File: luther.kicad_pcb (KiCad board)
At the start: 2 copper layers, 114 x 50 mm, 0 parts

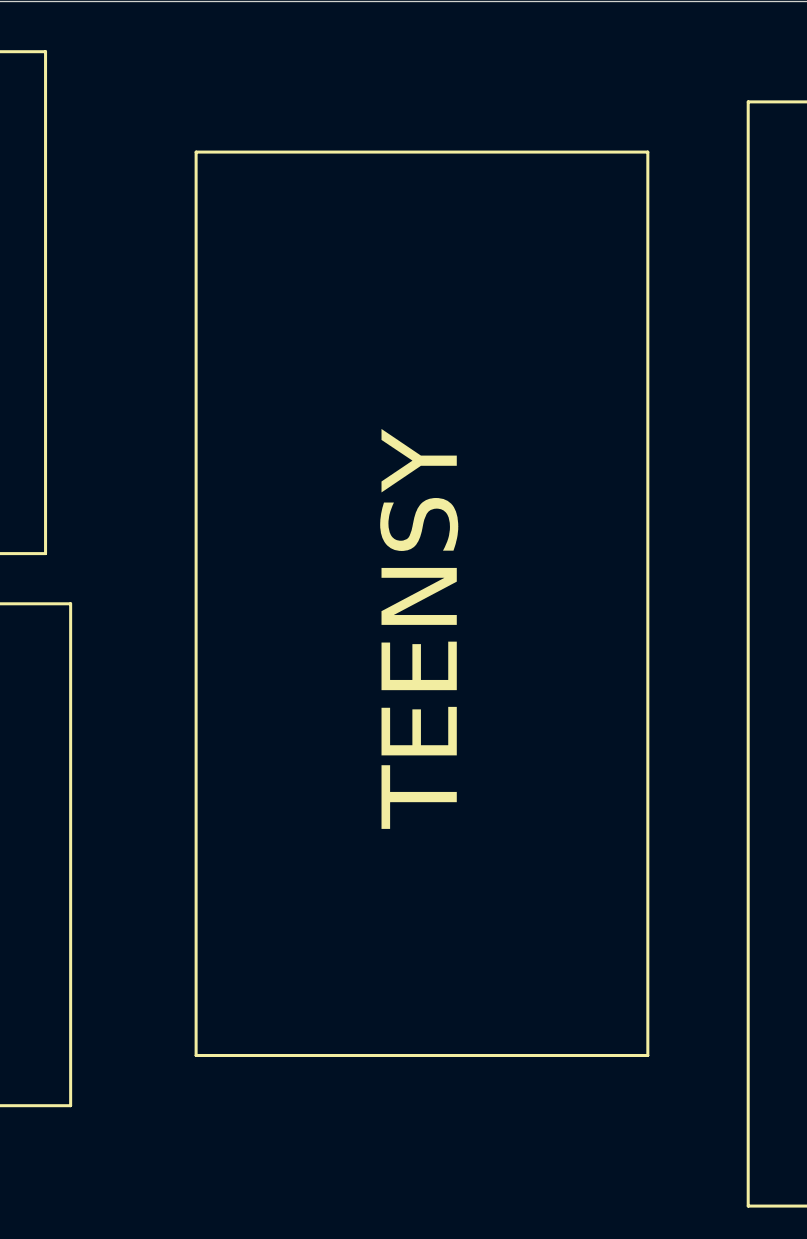
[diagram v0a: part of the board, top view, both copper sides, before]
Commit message: add teensy footprint
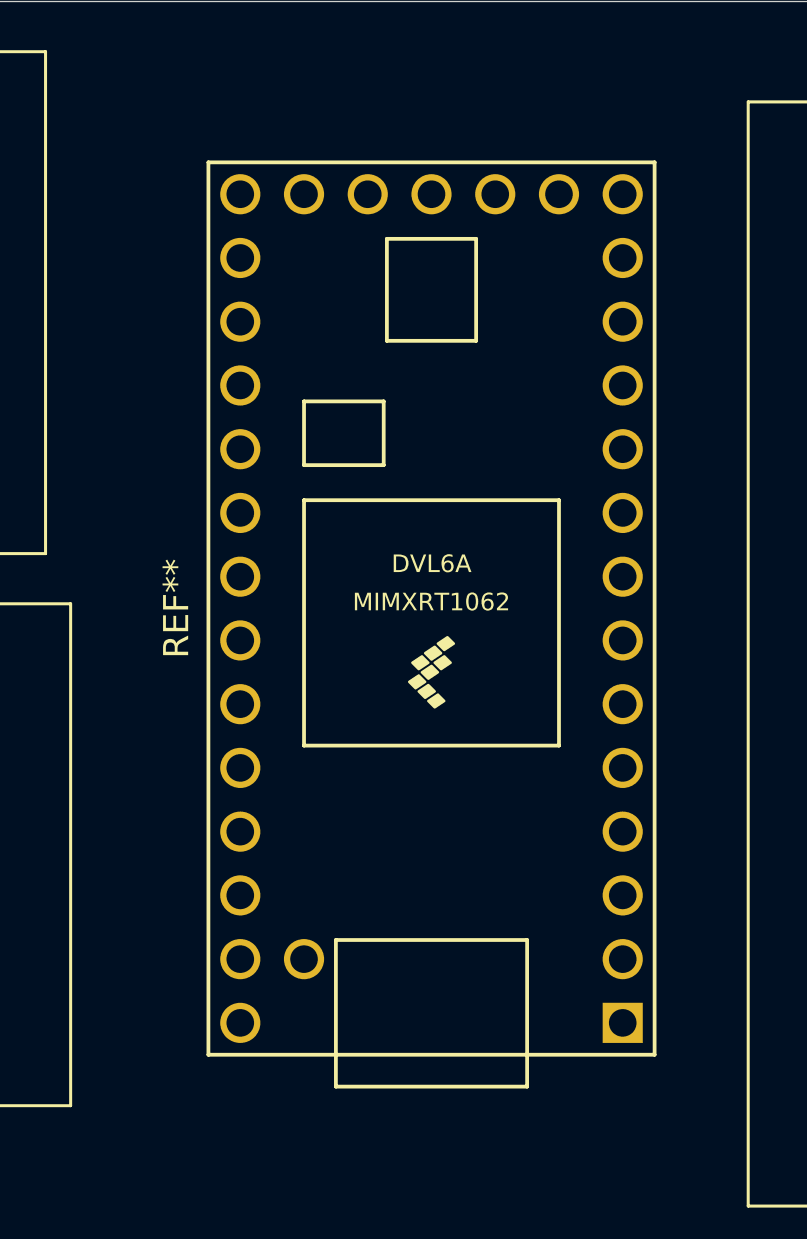
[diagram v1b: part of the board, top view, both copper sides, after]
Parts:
- added REF**: Teensy4.0, libs:Teensy40, F.Cu at (86.4, 94.2)
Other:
- board text removed: "TEENSY"
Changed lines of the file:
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@@
   (general
     (thickness 1.6)
-    (drawings 62)
+    (drawings 57)
     (tracks 0)
     (zones 0)
-    (modules 0)
+    (modules 1)
     (nets 1)
   )
@@
     (solder_mask_min_width 0.25)
     (aux_axis_origin 0 0)
-    (visible_elements FFFFFF7F)
+    (visible_elements 7FFFFFFF)
     (pcbplotparams
       (layerselection 0x010fc_ffffffff)
@@
     (uvia_drill 0.1)
   )
+  (module libs:Teensy40 (layer F.Cu)
+    (at 86.38 94.19 90)
+    (fp_text reference REF** (at 0 -10.16 90) (layer F.SilkS)
+      (effects (font (size 1 1) (thickness 0.15)))
+    )
+    (fp_text value Teensy4.0 (at 0 10.16 90) (layer F.Fab)
+      (effects (font (size 1 1) (thickness 0.15)))
+    )
+    (fp_text user DVL6A (at 1.778 0) (layer F.SilkS)
+      (effects (font (size 0.7 0.7) (thickness 0.15)))
+    )
+    (fp_poly (pts (xy -3.937 0.127) (xy -3.683 -0.127) (xy -3.429 0.254) (xy -3.683 0.508)) (layer F.SilkS) (width 0.1))
+    (fp_poly (pts (xy -3.556 -0.254) (xy -3.302 -0.508) (xy -3.048 -0.127) (xy -3.302 0.127)) (layer F.SilkS) (width 0.1))
+    (fp_poly (pts (xy -1.651 0.508) (xy -1.397 0.254) (xy -1.143 0.635) (xy -1.397 0.889)) (layer F.SilkS) (width 0.1))
+    (fp_poly (pts (xy -2.032 0) (xy -1.778 -0.254) (xy -1.524 0.127) (xy -1.778 0.381)) (layer F.SilkS) (width 0.1))
+    (fp_poly (pts (xy -2.413 -0.508) (xy -2.159 -0.762) (xy -1.905 -0.381) (xy -2.159 -0.127)) (layer F.SilkS) (width 0.1))
+    (fp_poly (pts (xy -2.413 0.381) (xy -2.159 0.127) (xy -1.905 0.508) (xy -2.159 0.762)) (layer F.SilkS) (width 0.1))
+    (fp_poly (pts (xy -2.794 -0.127) (xy -2.54 -0.381) (xy -2.286 0) (xy -2.54 0.254)) (layer F.SilkS) (width 0.1))
+    (fp_poly (pts (xy -3.175 -0.635) (xy -2.921 -0.889) (xy -2.667 -0.508) (xy -2.921 -0.254)) (layer F.SilkS) (width 0.1))
+    (fp_text user MIMXRT1062 (at 0.254 0) (layer F.SilkS)
+      (effects (font (size 0.7 0.7) (thickness 0.15)))
+    )
+    (fp_line (start 5.715 -1.905) (end 5.715 -5.08) (layer F.SilkS) (width 0.15))
+    (fp_line (start 8.255 -1.905) (end 5.715 -1.905) (layer F.SilkS) (width 0.15))
+    (fp_line (start 8.255 -5.08) (end 8.255 -1.905) (layer F.SilkS) (width 0.15))
+    (fp_line (start 5.715 -5.08) (end 8.255 -5.08) (layer F.SilkS) (width 0.15))
+    (fp_line (start -17.78 8.89) (end -17.78 -8.89) (layer F.SilkS) (width 0.15))
+    (fp_line (start 17.78 8.89) (end -17.78 8.89) (layer F.SilkS) (width 0.15))
+    (fp_line (start 17.78 -8.89) (end 17.78 8.89) (layer F.SilkS) (width 0.15))
+    (fp_line (start -17.78 -8.89) (end 17.78 -8.89) (layer F.SilkS) (width 0.15))
+    (fp_line (start 4.318 5.08) (end -5.461 5.08) (layer F.SilkS) (width 0.15))
+    (fp_line (start 4.318 -5.08) (end -5.461 -5.08) (layer F.SilkS) (width 0.15))
+    (fp_line (start -5.461 -5.08) (end -5.461 5.08) (layer F.SilkS) (width 0.15))
+    (fp_line (start 4.318 5.08) (end 4.318 -5.08) (layer F.SilkS) (width 0.15))
+    (fp_line (start 10.668 -1.778) (end 14.732 -1.778) (layer F.SilkS) (width 0.15))
+    (fp_line (start 10.668 1.778) (end 10.668 -1.778) (layer F.SilkS) (width 0.15))
+    (fp_line (start 14.732 1.778) (end 10.668 1.778) (layer F.SilkS) (width 0.15))
+    (fp_line (start 14.732 -1.778) (end 14.732 1.778) (layer F.SilkS) (width 0.15))
+    (fp_line (start -13.208 3.81) (end -17.78 3.81) (layer F.SilkS) (width 0.15))
+    (fp_line (start -13.208 -3.81) (end -17.78 -3.81) (layer F.SilkS) (width 0.15))
+    (fp_line (start -13.208 3.81) (end -13.208 -3.81) (layer F.SilkS) (width 0.15))
+    (fp_line (start -19.05 -3.81) (end -17.78 -3.81) (layer F.SilkS) (width 0.15))
+    (fp_line (start -19.05 3.81) (end -19.05 -3.81) (layer F.SilkS) (width 0.15))
+    (fp_line (start -17.78 3.81) (end -19.05 3.81) (layer F.SilkS) (width 0.15))
+    (pad 1 thru_hole rect (at -16.51 7.62 90) (size 1.6 1.6) (drill 1.1) (layers *.Cu *.Mask))
+    (pad 2 thru_hole circle (at -13.97 7.62 90) (size 1.6 1.6) (drill 1.1) (layers *.Cu *.Mask))
+    (pad 3 thru_hole circle (at -11.43 7.62 90) (size 1.6 1.6) (drill 1.1) (layers *.Cu *.Mask))
+    (pad 4 thru_hole circle (at -8.89 7.62 90) (size 1.6 1.6) (drill 1.1) (layers *.Cu *.Mask))
+    (pad 5 thru_hole circle (at -6.35 7.62 90) (size 1.6 1.6) (drill 1.1) (layers *.Cu *.Mask))
+    (pad 6 thru_hole circle (at -3.81 7.62 90) (size 1.6 1.6) (drill 1.1) (layers *.Cu *.Mask))
+    (pad 7 thru_hole circle (at -1.27 7.62 90) (size 1.6 1.6) (drill 1.1) (layers *.Cu *.Mask))
+    (pad 8 thru_hole circle (at 1.27 7.62 90) (size 1.6 1.6) (drill 1.1) (layers *.Cu *.Mask))
+    (pad 9 thru_hole circle (at 3.81 7.62 90) (size 1.6 1.6) (drill 1.1) (layers *.Cu *.Mask))
+    (pad 10 thru_hole circle (at 6.35 7.62 90) (size 1.6 1.6) (drill 1.1) (layers *.Cu *.Mask))
+    (pad 11 thru_hole circle (at 8.89 7.62 90) (size 1.6 1.6) (drill 1.1) (layers *.Cu *.Mask))
+    (pad 12 thru_hole circle (at 11.43 7.62 90) (size 1.6 1.6) (drill 1.1) (layers *.Cu *.Mask))
+    (pad 13 thru_hole circle (at 13.97 7.62 90) (size 1.6 1.6) (drill 1.1) (layers *.Cu *.Mask))
+    (pad 34 thru_hole circle (at -13.97 -5.08 90) (size 1.6 1.6) (drill 1.1) (layers *.Cu *.Mask))
+    (pad 33 thru_hole circle (at -16.51 -7.62 90) (size 1.6 1.6) (drill 1.1) (layers *.Cu *.Mask))
+    (pad 32 thru_hole circle (at -13.97 -7.62 90) (size 1.6 1.6) (drill 1.1) (layers *.Cu *.Mask))
+    (pad 31 thru_hole circle (at -11.43 -7.62 90) (size 1.6 1.6) (drill 1.1) (layers *.Cu *.Mask))
+    (pad 30 thru_hole circle (at -8.89 -7.62 90) (size 1.6 1.6) (drill 1.1) (layers *.Cu *.Mask))
+    (pad 29 thru_hole circle (at -6.35 -7.62 90) (size 1.6 1.6) (drill 1.1) (layers *.Cu *.Mask))
+    (pad 28 thru_hole circle (at -3.81 -7.62 90) (size 1.6 1.6) (drill 1.1) (layers *.Cu *.Mask))
+    (pad 27 thru_hole circle (at -1.27 -7.62 90) (size 1.6 1.6) (drill 1.1) (layers *.Cu *.Mask))
+    (pad 26 thru_hole circle (at 1.27 -7.62 90) (size 1.6 1.6) (drill 1.1) (layers *.Cu *.Mask))
+    (pad 25 thru_hole circle (at 3.81 -7.62 90) (size 1.6 1.6) (drill 1.1) (layers *.Cu *.Mask))
+    (pad 24 thru_hole circle (at 6.35 -7.62 90) (size 1.6 1.6) (drill 1.1) (layers *.Cu *.Mask))
+    (pad 23 thru_hole circle (at 8.89 -7.62 90) (size 1.6 1.6) (drill 1.1) (layers *.Cu *.Mask))
+    (pad 22 thru_hole circle (at 11.43 -7.62 90) (size 1.6 1.6) (drill 1.1) (layers *.Cu *.Mask))
+    (pad 21 thru_hole circle (at 13.97 -7.62 90) (size 1.6 1.6) (drill 1.1) (layers *.Cu *.Mask))
+    (pad 14 thru_hole circle (at 16.51 7.62 90) (size 1.6 1.6) (drill 1.1) (layers *.Cu *.Mask))
+    (pad 15 thru_hole circle (at 16.51 5.08 90) (size 1.6 1.6) (drill 1.1) (layers *.Cu *.Mask))
+    (pad 16 thru_hole circle (at 16.51 2.54 90) (size 1.6 1.6) (drill 1.1) (layers *.Cu *.Mask))
+    (pad 20 thru_hole circle (at 16.51 -7.62 90) (size 1.6 1.6) (drill 1.1) (layers *.Cu *.Mask))
+    (pad 19 thru_hole circle (at 16.51 -5.08 90) (size 1.6 1.6) (drill 1.1) (layers *.Cu *.Mask))
+    (pad 18 thru_hole circle (at 16.51 -2.54 90) (size 1.6 1.6) (drill 1.1) (layers *.Cu *.Mask))
+    (pad 17 thru_hole circle (at 16.51 0 90) (size 1.6 1.6) (drill 1.1) (layers *.Cu *.Mask))
+  )
   (dimension 114 (width 0.15) (layer Dwgs.User)
     (gr_text "114.000001 mm" (at 87 137.3) (layer Dwgs.User)
@@
   (gr_line (start 120 94) (end 120 119) (layer B.SilkS) (width 0.12))
   (gr_line (start 91 94) (end 120 94) (layer B.SilkS) (width 0.12))
-  (gr_text TEENSY (at 86 95 90) (layer F.SilkS)
-    (effects (font (size 3 3) (thickness 0.15)))
-  )
-  (gr_line (start 77 112) (end 95 112) (layer F.SilkS) (width 0.12))
-  (gr_line (start 77 76) (end 77 112) (layer F.SilkS) (width 0.12))
-  (gr_line (start 95 76) (end 77 76) (layer F.SilkS) (width 0.12))
-  (gr_line (start 95 112) (end 95 76) (layer F.SilkS) (width 0.12))
   (gr_text BNO (at 59 104 -90) (layer F.SilkS)
     (effects (font (size 3 3) (thickness 0.15)))

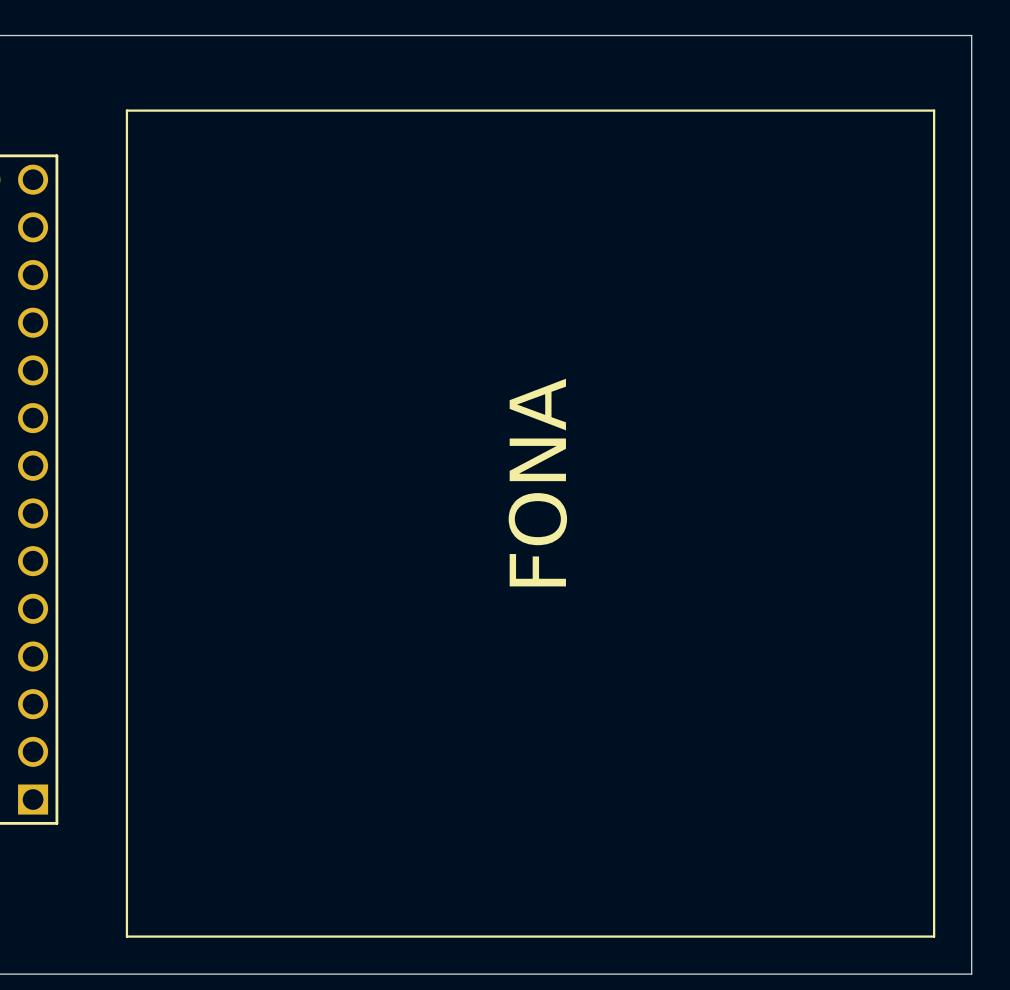
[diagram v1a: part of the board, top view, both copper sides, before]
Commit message: Some FONA808 stuff
I was gonna update the netlist on the PCB but then it said the changes you make cannot be undone and that psyched me out a little so I didn't but that seems like a good thing to do at some point perhaps
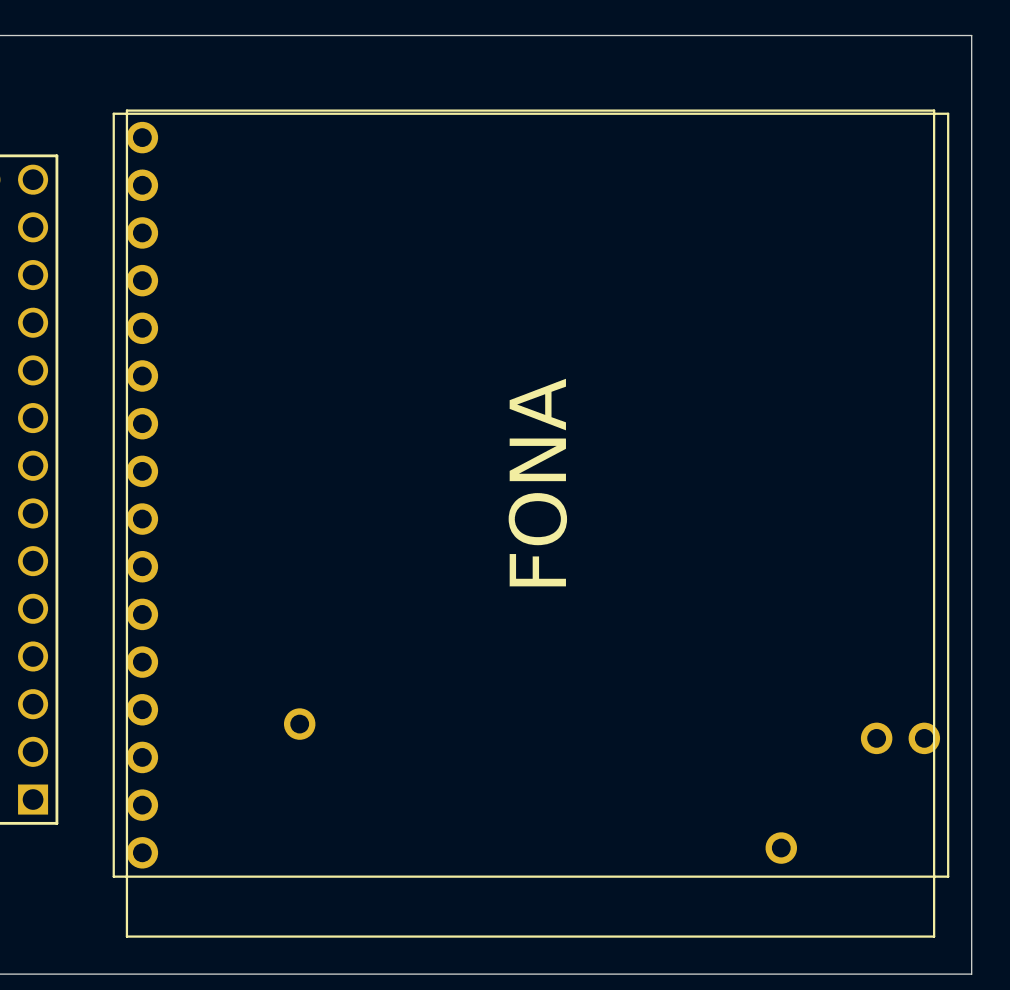
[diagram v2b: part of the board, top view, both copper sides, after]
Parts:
- added 1: FONA808, Adafruit SIM808 Breakout Copy:FONA808, F.Cu at (99.1, 74.2)
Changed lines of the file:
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@@
     (tracks 0)
     (zones 0)
-    (modules 1)
+    (modules 2)
     (nets 1)
   )
@@
     (uvia_dia 0.3)
     (uvia_drill 0.1)
+  )
+  (module "Adafruit SIM808 Breakout Copy:FONA808" (layer F.Cu)
+    (at 99.06 74.168)
+    (fp_text reference 1 (at 2.8448 -0.0762 270) (layer F.SilkS) hide
+      (effects (font (size 0.77216 0.77216) (thickness 0.138988)) (justify left bottom))
+    )
+    (fp_text value FONA808 (at -2.159 0 270) (layer F.Fab)
+      (effects (font (size 0.38608 0.38608) (thickness 0.038608)) (justify left bottom))
+    )
+    (fp_line (start 43.688 40.64) (end -0.762 40.64) (layer F.SilkS) (width 0.12))
+    (fp_line (start 43.688 0) (end 43.688 40.64) (layer F.SilkS) (width 0.12))
+    (fp_line (start -0.762 0) (end 43.688 0) (layer F.SilkS) (width 0.12))
+    (fp_line (start -0.762 0) (end -0.762 40.64) (layer F.SilkS) (width 0.12))
+    (fp_poly (pts (xy 0.762 39.116) (xy 0.762 39.624) (xy 1.27 39.624) (xy 1.27 39.116)) (layer F.Fab) (width 0))
+    (fp_poly (pts (xy 0.762 1.016) (xy 0.762 1.524) (xy 1.27 1.524) (xy 1.27 1.016)) (layer F.Fab) (width 0))
+    (fp_poly (pts (xy 0.762 3.556) (xy 0.762 4.064) (xy 1.27 4.064) (xy 1.27 3.556)) (layer F.Fab) (width 0))
+    (fp_poly (pts (xy 0.762 6.096) (xy 0.762 6.604) (xy 1.27 6.604) (xy 1.27 6.096)) (layer F.Fab) (width 0))
+    (fp_poly (pts (xy 0.762 8.636) (xy 0.762 9.144) (xy 1.27 9.144) (xy 1.27 8.636)) (layer F.Fab) (width 0))
+    (fp_poly (pts (xy 0.762 11.176) (xy 0.762 11.684) (xy 1.27 11.684) (xy 1.27 11.176)) (layer F.Fab) (width 0))
+    (fp_poly (pts (xy 0.762 13.716) (xy 0.762 14.224) (xy 1.27 14.224) (xy 1.27 13.716)) (layer F.Fab) (width 0))
+    (fp_poly (pts (xy 0.762 16.256) (xy 0.762 16.764) (xy 1.27 16.764) (xy 1.27 16.256)) (layer F.Fab) (width 0))
+    (fp_poly (pts (xy 0.762 18.796) (xy 0.762 19.304) (xy 1.27 19.304) (xy 1.27 18.796)) (layer F.Fab) (width 0))
+    (fp_poly (pts (xy 0.762 21.336) (xy 0.762 21.844) (xy 1.27 21.844) (xy 1.27 21.336)) (layer F.Fab) (width 0))
+    (fp_poly (pts (xy 0.762 23.876) (xy 0.762 24.384) (xy 1.27 24.384) (xy 1.27 23.876)) (layer F.Fab) (width 0))
+    (fp_poly (pts (xy 0.762 26.416) (xy 0.762 26.924) (xy 1.27 26.924) (xy 1.27 26.416)) (layer F.Fab) (width 0))
+    (fp_poly (pts (xy 0.762 28.956) (xy 0.762 29.464) (xy 1.27 29.464) (xy 1.27 28.956)) (layer F.Fab) (width 0))
+    (fp_poly (pts (xy 0.762 31.496) (xy 0.762 32.004) (xy 1.27 32.004) (xy 1.27 31.496)) (layer F.Fab) (width 0))
+    (fp_poly (pts (xy 0.762 34.036) (xy 0.762 34.544) (xy 1.27 34.544) (xy 1.27 34.036)) (layer F.Fab) (width 0))
+    (fp_poly (pts (xy 0.762 36.576) (xy 0.762 37.084) (xy 1.27 37.084) (xy 1.27 36.576)) (layer F.Fab) (width 0))
+    (fp_line (start 1.651 0) (end 0.381 0) (layer F.Fab) (width 0.2032))
+    (pad 20 thru_hole circle (at 9.144 32.512 270) (size 1.676 1.676) (drill 1) (layers *.Cu *.Mask))
+    (pad 19 thru_hole circle (at 34.798 39.116 270) (size 1.676 1.676) (drill 1) (layers *.Cu *.Mask))
+    (pad 18 thru_hole circle (at 39.878 33.274 270) (size 1.676 1.676) (drill 1) (layers *.Cu *.Mask))
+    (pad 17 thru_hole circle (at 42.418 33.274 270) (size 1.676 1.676) (drill 1) (layers *.Cu *.Mask))
+    (pad 16 thru_hole circle (at 0.762 39.37) (size 1.6764 1.6764) (drill 1) (layers *.Cu *.Mask)
+      (solder_mask_margin 0.0508))
+    (pad 15 thru_hole circle (at 0.762 36.83) (size 1.6764 1.6764) (drill 1) (layers *.Cu *.Mask)
+      (solder_mask_margin 0.0508))
+    (pad 14 thru_hole circle (at 0.762 34.29) (size 1.6764 1.6764) (drill 1) (layers *.Cu *.Mask)
+      (solder_mask_margin 0.0508))
+    (pad 13 thru_hole circle (at 0.762 31.75) (size 1.6764 1.6764) (drill 1) (layers *.Cu *.Mask)
+      (solder_mask_margin 0.0508))
+    (pad 12 thru_hole circle (at 0.762 29.21) (size 1.6764 1.6764) (drill 1) (layers *.Cu *.Mask)
+      (solder_mask_margin 0.0508))
+    (pad 11 thru_hole circle (at 0.762 26.67) (size 1.6764 1.6764) (drill 1) (layers *.Cu *.Mask)
+      (solder_mask_margin 0.0508))
+    (pad 10 thru_hole circle (at 0.762 24.13) (size 1.6764 1.6764) (drill 1) (layers *.Cu *.Mask)
+      (solder_mask_margin 0.0508))
+    (pad 9 thru_hole circle (at 0.762 21.59) (size 1.6764 1.6764) (drill 1) (layers *.Cu *.Mask)
+      (solder_mask_margin 0.0508))
+    (pad 8 thru_hole circle (at 0.762 19.05) (size 1.6764 1.6764) (drill 1) (layers *.Cu *.Mask)
+      (solder_mask_margin 0.0508))
+    (pad 7 thru_hole circle (at 0.762 16.51) (size 1.6764 1.6764) (drill 1) (layers *.Cu *.Mask)
+      (solder_mask_margin 0.0508))
+    (pad 6 thru_hole circle (at 0.762 13.97) (size 1.6764 1.6764) (drill 1) (layers *.Cu *.Mask)
+      (solder_mask_margin 0.0508))
+    (pad 5 thru_hole circle (at 0.762 11.43) (size 1.6764 1.6764) (drill 1) (layers *.Cu *.Mask)
+      (solder_mask_margin 0.0508))
+    (pad 4 thru_hole circle (at 0.762 8.89) (size 1.6764 1.6764) (drill 1) (layers *.Cu *.Mask)
+      (solder_mask_margin 0.0508))
+    (pad 3 thru_hole circle (at 0.762 6.35) (size 1.6764 1.6764) (drill 1) (layers *.Cu *.Mask)
+      (solder_mask_margin 0.0508))
+    (pad 2 thru_hole circle (at 0.762 3.81) (size 1.6764 1.6764) (drill 1) (layers *.Cu *.Mask)
+      (solder_mask_margin 0.0508))
+    (pad 1 thru_hole circle (at 0.762 1.27) (size 1.6764 1.6764) (drill 1) (layers *.Cu *.Mask)
+      (solder_mask_margin 0.0508))
   )
   (module libs:Teensy40 (layer F.Cu)
@@
     (pad 17 thru_hole circle (at 16.51 0 90) (size 1.6 1.6) (drill 1.1) (layers *.Cu *.Mask))
   )
+  (gr_text FONA (at 121 94 90) (layer F.SilkS)
+    (effects (font (size 3 3) (thickness 0.15)))
+  )
   (dimension 114 (width 0.15) (layer Dwgs.User)
     (gr_text "114.000001 mm" (at 87 137.3) (layer Dwgs.User)
@@
   (gr_line (start 45 114) (end 72 114) (layer F.SilkS) (width 0.12))
   (gr_line (start 45 94) (end 45 114) (layer F.SilkS) (width 0.12))
-  (gr_text FONA (at 121 94 90) (layer F.SilkS)
-    (effects (font (size 3 3) (thickness 0.15)))
-  )
   (gr_line (start 99 118) (end 142 118) (layer F.SilkS) (width 0.12))
   (gr_line (start 99 74) (end 99 118) (layer F.SilkS) (width 0.12))
